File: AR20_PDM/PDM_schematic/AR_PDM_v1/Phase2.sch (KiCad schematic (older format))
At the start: 12 parts, among them Q2 BTS50025-1TAD, U9 INA233

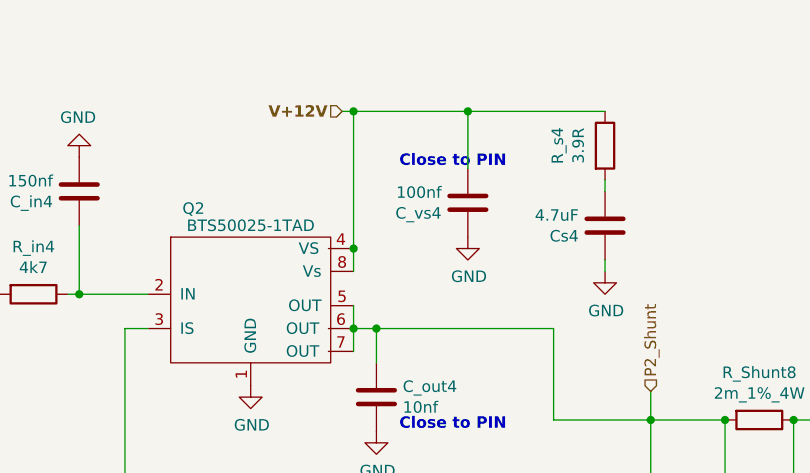
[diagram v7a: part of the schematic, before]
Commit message: First Complete Draft of PCB and schematics, - minus see discription
- missing correct smd switch header
- missing correct main power plug
- tweeks still needs to be done
- Extra inspection of schematics pending
- proper, in depth quiality controll of pcb work pending
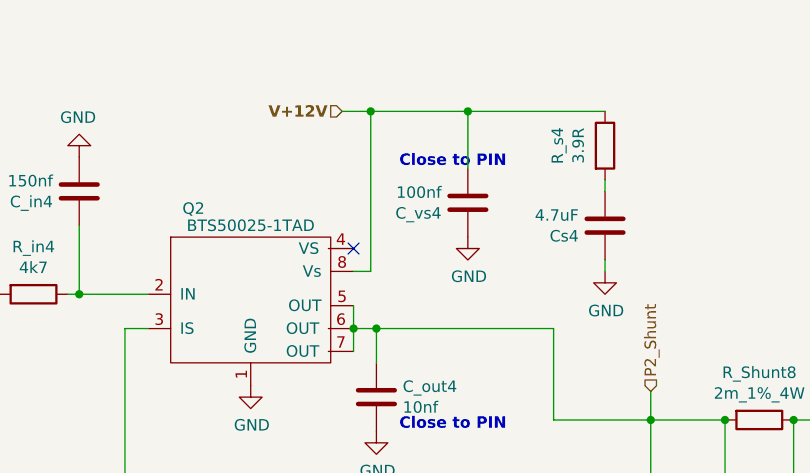
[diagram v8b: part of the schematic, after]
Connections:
- net V+12V: no longer Q2.4 (VS)
- no-connect marks 0 -> 1
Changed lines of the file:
@@
 $Descr A4 11693 8268
 encoding utf-8
-Sheet 7 13
+Sheet 6 13
 Title ""
 Date ""
@@
 $EndComp
 Wire Wire Line
-	4700 2550 4800 2550
-Wire Wire Line
 	4800 2550 4800 2700
 $Comp
@@
 	3500 2400 3800 2400
 $Comp
-L AR20_PDM_v1-rescue:BTS50025-1TAD Q?
-U 1 1 5E21B7FD
-P 4250 2650
-AR Path="/5DA89415/5E21B7FD" Ref="Q?"  Part="1"
-AR Path="/5DEB10A1/5E21B7FD" Ref="Q?"  Part="1"
-AR Path="/5DEB20EA/5E21B7FD" Ref="Q?"  Part="1"
-AR Path="/5E0E4725/5E21B7FD" Ref="Q?"  Part="1"
-AR Path="/5E0E4A93/5E21B7FD" Ref="Q?"  Part="1"
-AR Path="/5E0E4EB5/5E21B7FD" Ref="Q?"  Part="1"
-AR Path="/5E0E5304/5E21B7FD" Ref="Q?"  Part="1"
-AR Path="/5E0E594B/5E21B7FD" Ref="Q?"  Part="1"
-AR Path="/5E0E607C/5E21B7FD" Ref="Q?"  Part="1"
-AR Path="/5E0FB5C8/5E21B7FD" Ref="Q2"  Part="1"
-AR Path="/5E0FBBBD/5E21B7FD" Ref="Q?"  Part="1"
-AR Path="/5E0FC3A2/5E21B7FD" Ref="Q?"  Part="1"
-AR Path="/5E0FCFDC/5E21B7FD" Ref="Q?"  Part="1"
-AR Path="/5E0FDCCC/5E21B7FD" Ref="Q?"  Part="1"
-AR Path="/5E10174B/5E21B7FD" Ref="Q?"  Part="1"
-F 0 "Q2" H 4000 3275 50  0000 C CNN
-F 1 "BTS50025-1TAD" H 4250 3200 50  0000 C CNN
-F 2 "AR_PDM_v1:BTS500xx" H 4250 2650 50  0001 C CNN
-F 3 "" H 4250 2650 50  0001 C CNN
-	1    4250 2650
-	1    0    0    -1
-$EndComp
-$Comp
 L AR20_PDM_v1-rescue:INA233 U?
 U 1 1 5E21B802
@@
 Text HLabel 10000 4900 3    50   Input ~ 10
 vcc_5v
-Wire Wire Line
-	4650 1600 4700 1600
-Wire Wire Line
-	4700 2300 4700 2200
-Wire Wire Line
-	4700 2200 4700 1600
-Connection ~ 4700 2200
-Connection ~ 4700 1600
-Wire Wire Line
-	4700 1600 5200 1600
 Connection ~ 4700 2550
 Wire Wire Line
@@
 Wire Wire Line
 	3700 2550 3700 3300
+Wire Wire Line
+	4650 1600 4775 1600
+Wire Wire Line
+	4700 2550 4800 2550
+$Comp
+L AR20_PDM_v1-rescue:BTS50025-1TAD Q?
+U 1 1 5E21B7FD
+P 4250 2650
+AR Path="/5DA89415/5E21B7FD" Ref="Q?"  Part="1"
+AR Path="/5DEB10A1/5E21B7FD" Ref="Q?"  Part="1"
+AR Path="/5DEB20EA/5E21B7FD" Ref="Q?"  Part="1"
+AR Path="/5E0E4725/5E21B7FD" Ref="Q?"  Part="1"
+AR Path="/5E0E4A93/5E21B7FD" Ref="Q?"  Part="1"
+AR Path="/5E0E4EB5/5E21B7FD" Ref="Q?"  Part="1"
+AR Path="/5E0E5304/5E21B7FD" Ref="Q?"  Part="1"
+AR Path="/5E0E594B/5E21B7FD" Ref="Q?"  Part="1"
+AR Path="/5E0E607C/5E21B7FD" Ref="Q?"  Part="1"
+AR Path="/5E0FB5C8/5E21B7FD" Ref="Q2"  Part="1"
+AR Path="/5E0FBBBD/5E21B7FD" Ref="Q?"  Part="1"
+AR Path="/5E0FC3A2/5E21B7FD" Ref="Q?"  Part="1"
+AR Path="/5E0FCFDC/5E21B7FD" Ref="Q?"  Part="1"
+AR Path="/5E0FDCCC/5E21B7FD" Ref="Q?"  Part="1"
+AR Path="/5E10174B/5E21B7FD" Ref="Q?"  Part="1"
+F 0 "Q2" H 4000 3275 50  0000 C CNN
+F 1 "BTS50025-1TAD" H 4250 3200 50  0000 C CNN
+F 2 "AR_PDM_v1:BTS500xx" H 4250 2650 50  0001 C CNN
+F 3 "" H 4250 2650 50  0001 C CNN
+	1    4250 2650
+	1    0    0    -1
+$EndComp
+Wire Wire Line
+	4775 2300 4700 2300
+Wire Wire Line
+	4775 1600 4775 2300
+NoConn ~ 4700 2200
+Connection ~ 4775 1600
+Wire Wire Line
+	4775 1600 5200 1600
 $EndSCHEMATC
